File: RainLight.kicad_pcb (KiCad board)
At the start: 2 copper layers, 120 x 55 mm, 25 parts, among them J1 DTM04-2P (wire pigtail)

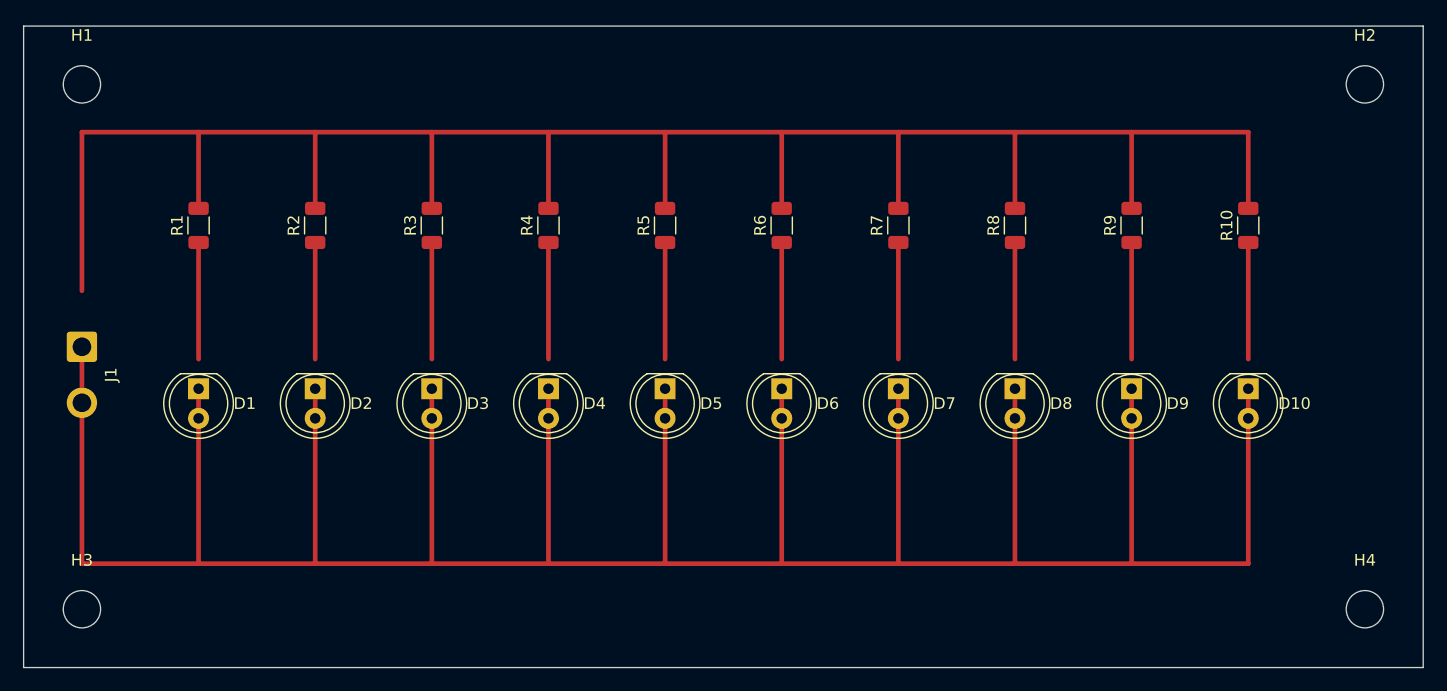
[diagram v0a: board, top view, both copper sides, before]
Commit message: PCB: honeycomb 3-row layout (3-4-3 staggered), VCC on F.Cu / GND on B.Cu to avoid trace crossings, 4x M3 mounting holes
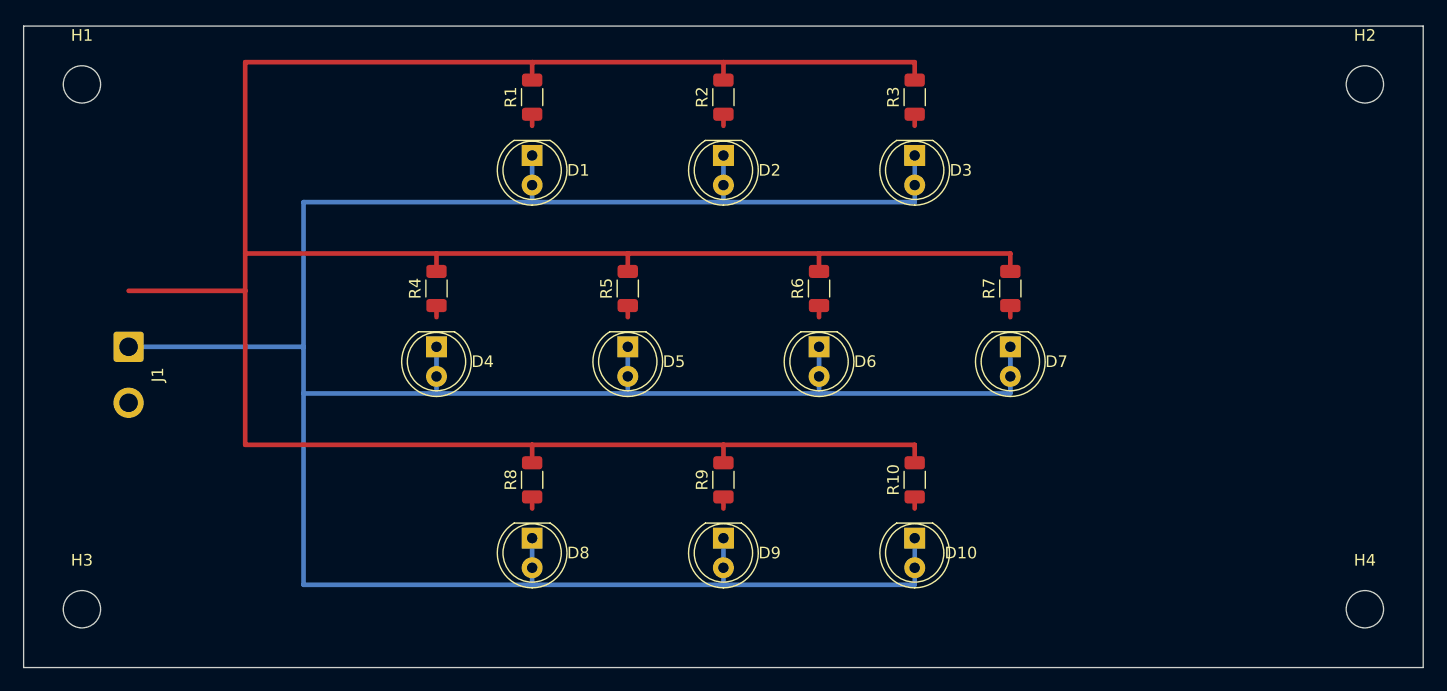
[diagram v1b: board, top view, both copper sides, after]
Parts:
- moved R8 46.8 mm to (124.6, 119.8)
- moved D3 46.0 mm to (157.4, 92.0)
- moved D8 43.3 mm to (124.6, 124.8)
- moved R3 42.8 mm to (157.4, 87.0)
- moved R9 41.2 mm to (141.0, 119.8)
- moved D2 40.3 mm to (141.0, 92.0)
- moved D9 37.3 mm to (141.0, 124.8)
- moved R2 36.7 mm to (141.0, 87.0)
- moved R10 36.0 mm to (157.4, 119.8)
- moved D1 34.9 mm to (124.6, 92.0)
- moved D10 31.3 mm to (157.4, 124.8)
- moved R1 30.6 mm to (124.6, 87.0)
- moved R4 11.0 mm to (116.4, 103.4)
- moved R7 11.0 mm to (165.6, 103.4)
- moved D4 10.3 mm to (116.4, 108.4)
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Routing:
- net VCC: track 179.0 -> 238.6 mm
- net GND: track 268.6 -> 253.2 mm
- net Net-(D9-A): track 10.00 -> 1.00 mm
- net Net-(D8-A): track 10.00 -> 1.00 mm
- net Net-(D7-A): track 10.00 -> 1.00 mm
- net Net-(D6-A): track 10.00 -> 1.00 mm
- net Net-(D5-A): track 10.00 -> 1.00 mm
- net Net-(D4-A): track 10.00 -> 1.00 mm
- net Net-(D3-A): track 10.00 -> 1.00 mm
- net Net-(D2-A): track 10.00 -> 1.00 mm
- net Net-(D10-A): track 10.00 -> 1.00 mm
- net Net-(D1-A): track 10.00 -> 1.00 mm

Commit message: PCB: switch R1-R10 from SMD 1206 to THT axial (DIN0207, 1/4W, vertical), increase resistor-to-LED clearance to 6.5mm
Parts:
- R1, R10, R2, R3, R4, R5, R6, R7, R8, R9: footprint Resistor_SMD:R_1206_3216Metric -> Resistor_THT:R_Axial_DIN0207_L6.3mm_D2.5mm_P2.54mm_Vertical
- moved R1 1.50 mm to (124.6, 85.5)
- moved R10 1.50 mm to (157.4, 118.3)
- moved R2 1.50 mm to (141.0, 85.5)
- moved R3 1.50 mm to (157.4, 85.5)
- moved R4 1.50 mm to (116.4, 101.9)
- moved R5 1.50 mm to (132.8, 101.9)
- moved R6 1.50 mm to (149.2, 101.9)
- moved R7 1.50 mm to (165.6, 101.9)
- moved R8 1.50 mm to (124.6, 118.3)
- moved R9 1.50 mm to (141.0, 118.3)
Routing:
- net VCC: track 238.6 -> 253.2 mm
